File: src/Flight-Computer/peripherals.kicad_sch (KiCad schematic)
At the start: 26 parts, among them P3 USB, P4 282837-6, Q1 QS5U17TR, Q2 QS5U17TR, U3 CP2102-GMR(QFN28), U4 SST25VF040B-50-4I-S2AE-T, U5 TS391IYLT, U6 TS391IYLT, U7 TS391IYLT

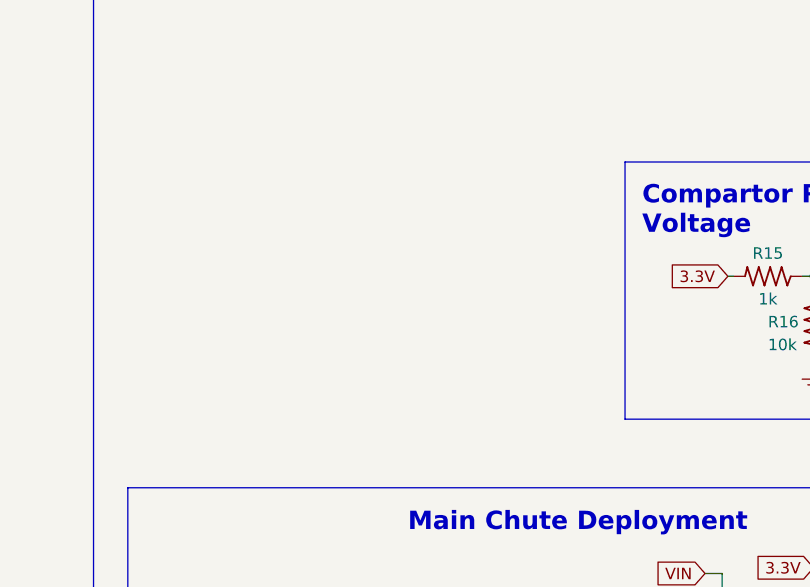
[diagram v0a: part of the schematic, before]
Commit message: implemented buzzer in schematic
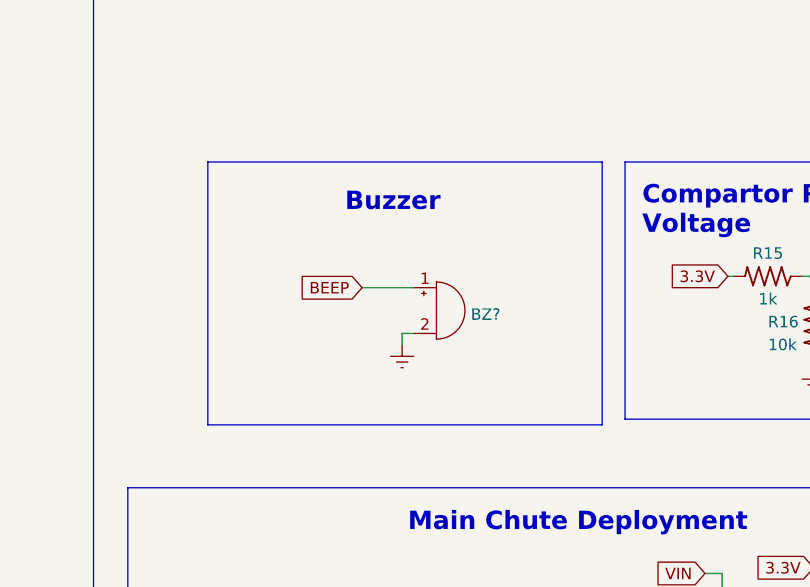
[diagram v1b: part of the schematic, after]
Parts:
- added BZ?: AT-1438-TWT-R, symbol Flight-Computer:AT-1438-TWT-R
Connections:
- net Earth: now also BZ?.2 (+)
- new net BEEP: BZ?.1 (-)
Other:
- note added: "Buzzer"
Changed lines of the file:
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@@
+    (stroke (width 0) (type default) (color 0 0 0 0))
+  )
+  (polyline (pts (xy 186.055 42.545) (xy 229.87 42.545))
     (stroke (width 0) (type default) (color 0 0 0 0))
   )
@@
     (stroke (width 0) (type default) (color 0 0 0 0))
   )
+  (wire (pts (xy 207.645 61.595) (xy 207.645 62.865))
+    (stroke (width 0) (type default) (color 0 0 0 0))
+  )
   (wire (pts (xy 253.365 55.245) (xy 253.365 56.515))
     (stroke (width 0) (type default) (color 0 0 0 0))
@@
     (stroke (width 0) (type default) (color 0 0 0 0))
   )
+  (polyline (pts (xy 186.055 42.545) (xy 186.055 71.755))
+    (stroke (width 0) (type default) (color 0 0 0 0))
+  )
   (wire (pts (xy 123.825 75.565) (xy 133.985 75.565))
     (stroke (width 0) (type default) (color 0 0 0 0))
@@
     (stroke (width 0) (type default) (color 0 0 0 0))
   )
+  (wire (pts (xy 208.915 61.595) (xy 207.645 61.595))
+    (stroke (width 0) (type default) (color 0 0 0 0))
+  )
   (wire (pts (xy 254 142.875) (xy 257.81 142.875))
     (stroke (width 0) (type default) (color 0 0 0 0))
@@
     (stroke (width 0) (type default) (color 0 0 0 0))
   )
+  (polyline (pts (xy 229.87 71.755) (xy 186.055 71.755))
+    (stroke (width 0) (type default) (color 0 0 0 0))
+  )
   (wire (pts (xy 243.205 106.68) (xy 243.205 107.95))
     (stroke (width 0) (type default) (color 0 0 0 0))
@@
     (stroke (width 0) (type default) (color 0 0 0 0))
   )
+  (polyline (pts (xy 229.87 42.545) (xy 229.87 71.755))
+    (stroke (width 0) (type default) (color 0 0 0 0))
+  )
   (polyline (pts (xy 89.535 94.615) (xy 173.355 94.615))
     (stroke (width 0) (type default) (color 0 0 0 0))
@@
   )
   (wire (pts (xy 57.785 46.99) (xy 59.69 46.99))
+    (stroke (width 0) (type default) (color 0 0 0 0))
+  )
+  (wire (pts (xy 203.2 56.515) (xy 208.915 56.515))
     (stroke (width 0) (type default) (color 0 0 0 0))
   )
@@
   )
   (text "Drogue Chute Deployment" (at 208.28 127 0)
+    (effects (font (size 2.032 2.032) (thickness 0.4064) bold) (justify left bottom))
+  )
+  (text "Buzzer" (at 201.295 48.26 0)
     (effects (font (size 2.032 2.032) (thickness 0.4064) bold) (justify left bottom))
   )
@@
     (property "Intersheet References" "${INTERSHEET_REFS}" (id 0) (at 64.3123 46.9106 0)
       (effects (font (size 1.27 1.27)) (justify left) hide)
+    )
+  )
+  (global_label "BEEP" (shape input) (at 203.2 56.515 180) (fields_autoplaced)
+    (effects (font (size 1.27 1.27)) (justify right))
+    (property "Intersheet References" "${INTERSHEET_REFS}" (id 0) (at 196.0377 56.4356 0)
+      (effects (font (size 1.27 1.27)) (justify right) hide)
     )
   )
@@
     (property "Datasheet" "" (id 3) (at 216.535 109.22 0)
       (effects (font (size 1.27 1.27)) (justify left bottom) hide)
+    )
+    (pin "1")
+    (pin "2")
+  )
+  (symbol (lib_id "Flight-Computer:AT-1438-TWT-R") (at 211.455 59.055 0) (unit 1)
+    (in_bom yes) (on_board yes) (fields_autoplaced)
+    (property "Reference" "BZ?" (id 0) (at 215.265 59.4888 0)
+      (effects (font (size 1.27 1.27)) (justify left))
+    )
+    (property "Value" "AT-1438-TWT-R" (id 1) (at 215.265 60.325 0)
+      (effects (font (size 1.27 1.27)) (justify left) hide)
+    )
+    (property "Footprint" "" (id 2) (at 210.82 56.515 90)
+      (effects (font (size 1.27 1.27)) hide)
+    )
+    (property "Datasheet" "~" (id 3) (at 210.82 56.515 90)
+      (effects (font (size 1.27 1.27)) hide)
     )
     (pin "1")
@@
     (pin "5")
   )
+  (symbol (lib_id "Flight-Computer:Earth") (at 207.645 62.865 0) (unit 1)
+    (in_bom yes) (on_board yes) (fields_autoplaced)
+    (property "Reference" "#PWR?" (id 0) (at 207.645 69.215 0)
+      (effects (font (size 1.27 1.27)) hide)
+    )
+    (property "Value" "Earth" (id 1) (at 207.645 66.675 0)
+      (effects (font (size 1.27 1.27)) hide)
+    )
+    (property "Footprint" "" (id 2) (at 207.645 62.865 0)
+      (effects (font (size 1.27 1.27)) hide)
+    )
+    (property "Datasheet" "" (id 3) (at 207.645 62.865 0)
+      (effects (font (size 1.27 1.27)) hide)
+    )
+    (pin "1")
+  )
   (symbol (lib_id "Flight-Computer:Earth") (at 207.01 156.845 0) (unit 1)

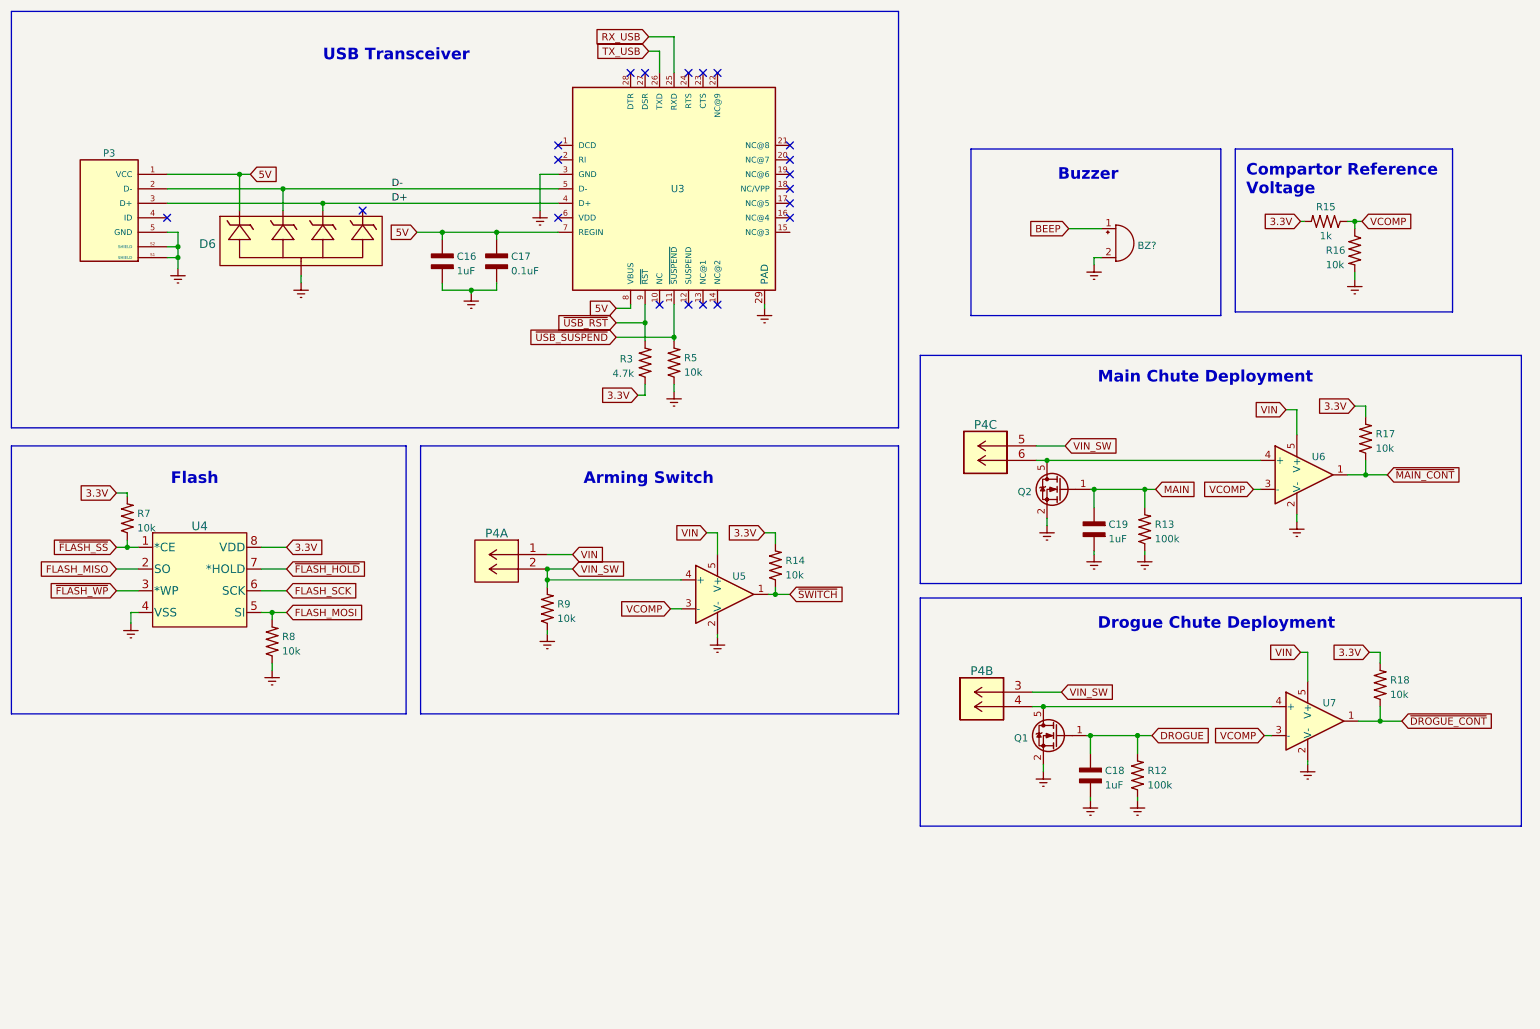
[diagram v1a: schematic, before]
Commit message: added RF SMA connector to lib files
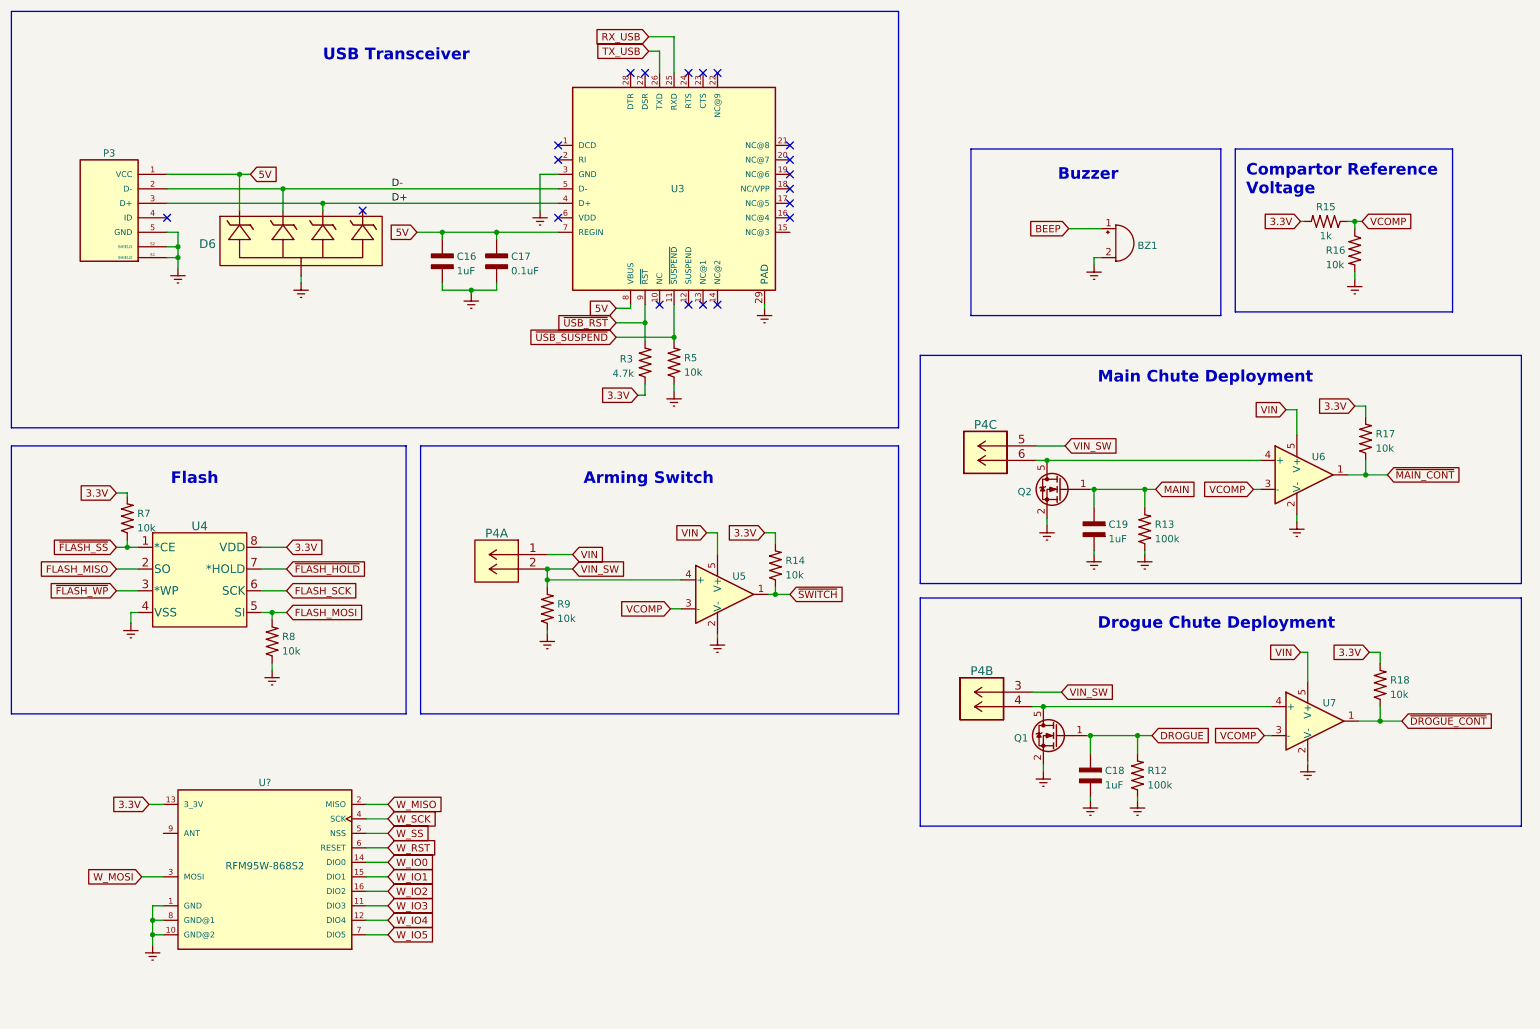
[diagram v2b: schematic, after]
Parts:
- added U?: RFM95W-868S2, XCVR_RFM95W-868S2, symbol Flight-Computer:RFM95W-868S2
- gave numbers to parts that had none: 1
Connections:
- net 3.3V: now also U?.13 (3_3V)
- net Earth: now also U?.1 (GND), U?.10 (GND@2), U?.8 (GND@1)
- new net W_IO0: U?.14 (DIO0)
- new net W_IO1: U?.15 (DIO1)
- new net W_IO2: U?.16 (DIO2)
- new net W_IO3: U?.11 (DIO3)
- new net W_IO4: U?.12 (DIO4)
- new net W_IO5: U?.7 (DIO5)
- new net W_MISO: U?.2 (MISO)
- new net W_MOSI: U?.3 (MOSI)
- new net W_RST: U?.6 (RESET)
- new net W_SCK: U?.4 (SCK)
- new net W_SS: U?.5 (NSS)

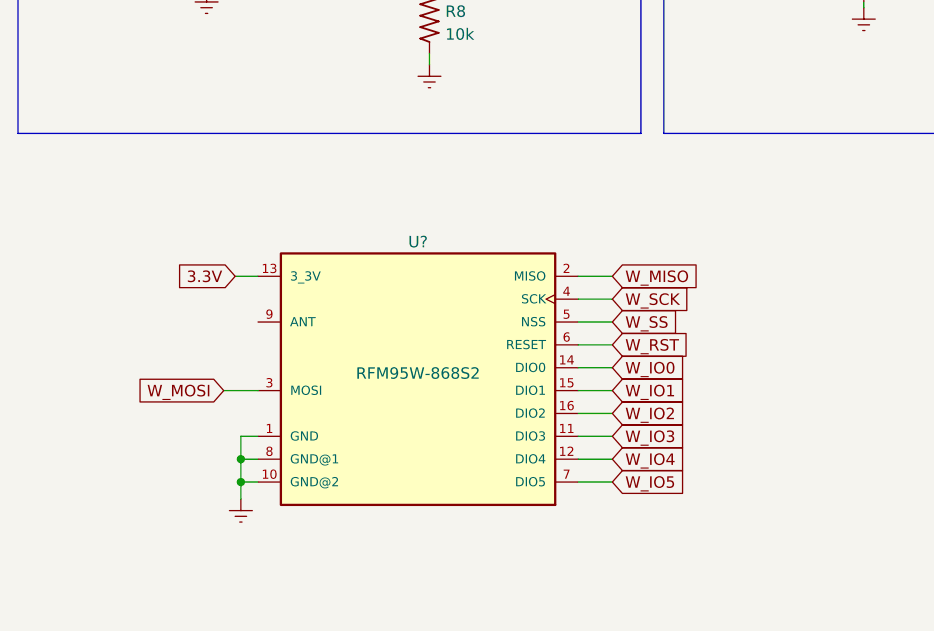
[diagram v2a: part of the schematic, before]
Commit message: implemented lora module in schematic
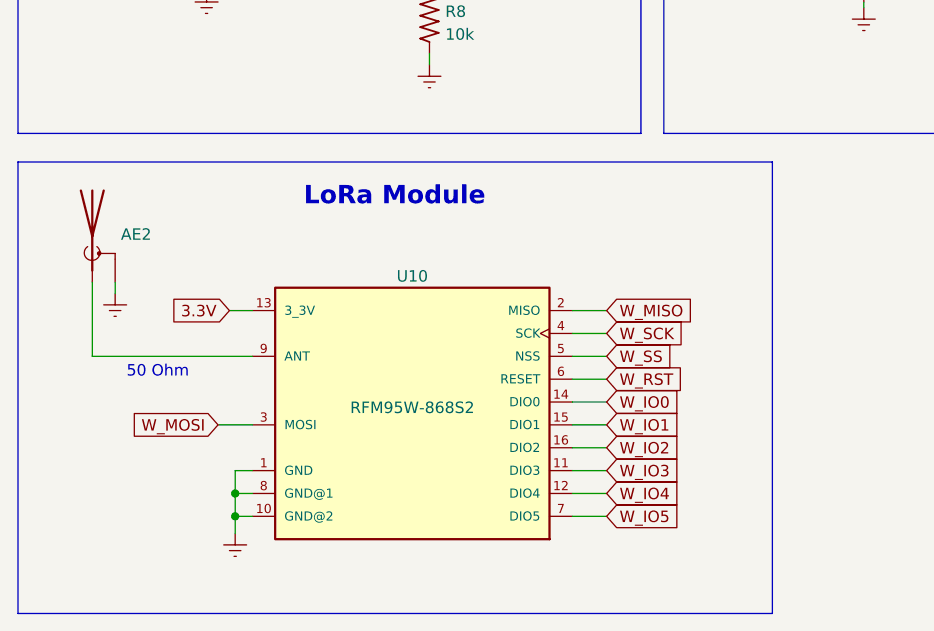
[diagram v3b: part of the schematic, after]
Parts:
- added AE2: 142-0701-851, symbol Flight-Computer:142-0701-851
- gave numbers to parts that had none: 1
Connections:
- net Earth: now also AE2.2 (Shield)
- net at U10.9 (ANT): now also AE2.1 (A)
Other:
- note added: "50 Ohm"
- note added: "LoRa Module"
- moved on the sheet: U10
